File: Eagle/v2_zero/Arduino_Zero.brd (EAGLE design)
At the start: 81.3 x 36.8 mm, 73 parts, among them IC1 74HC125D, IC2 MAX31855, IC3 MAX31855, IC4 REG1117, IC5 ATSAMD21G-A, IC6 SPX3819-3.3, IC7 TXS0108E, IC8 TLP283, J3 USB-MICROB, J4 NM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

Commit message: update 3d packages
small updates
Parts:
- removed C18: 1uF, rcl:C0603K
- removed C20: 4.7uF, rcl:C0603K
- added C3, C9: TAJB106K020RNJ, microbuilder:CAPMP3528X210N
- IC8: device optocoupler:MINI-FLAT-4 -> gfe-hand-made:SO4_TOS
- moved IC8 53.6 mm to (8.41, -10.5)
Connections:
- net +5V: now also C9.1; no longer C20.1
- net 12V: now also C3.1; no longer C18.1
- net GND: now also C3.2, C9.2; no longer C18.2, C20.2, IC8.2
- net N$12: no longer IC8.1
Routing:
- net N$32: track 2.73 -> 4.65 mm
- net N$14: track 7.97 -> 6.28 mm
- net +5V: track 185.5 -> 186.6 mm
- net 12V: track 64.7 -> 65.8 mm
- net N$12: track 19.8 -> 18.9 mm
- net D5_LCD_DB5: track 28.4 -> 27.9 mm

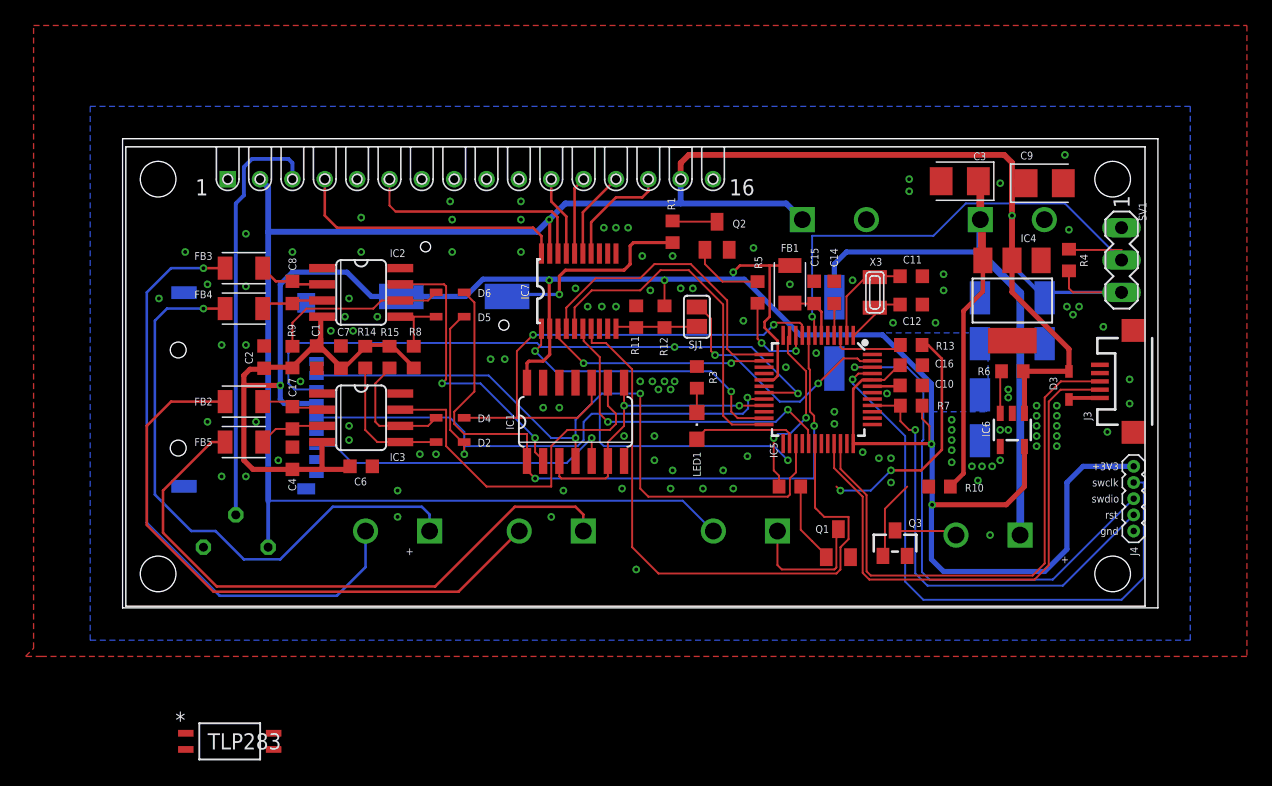
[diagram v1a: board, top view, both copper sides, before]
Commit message: schematic update
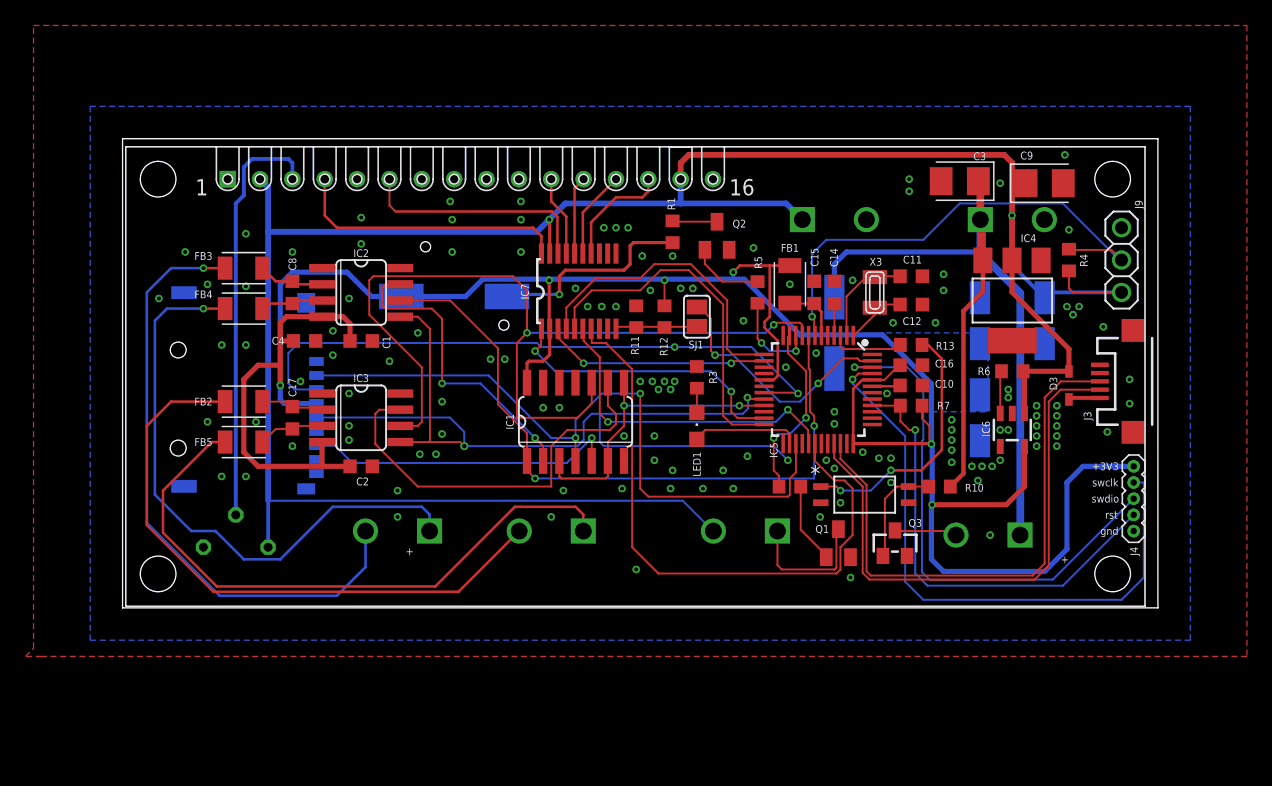
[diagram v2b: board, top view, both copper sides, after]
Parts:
- removed C6, C7: 10uF, rcl:C0603K
- removed D2, D4, D5, D6: 1N4148, adafruit:SOD323
- removed R14, R15, R8, R9: 10K, rcl:R0603
- removed SV1: (no value), con-lstb:MA03-1
- added J9: (no value), adafruit:1X03
- moved IC8 53.5 mm to (58.3, 8.89)
- moved C2 11.5 mm to (18.7, 11.1), turned to 0 degrees
- moved C4 9.26 mm to (14.3, 21.0), turned to 0 degrees
- moved C1 3.72 mm to (18.7, 21.0), turned to 0 degrees
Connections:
- removed net CS1: D4.2, IC3.6, R15.2
- removed net CS2: D6.2, IC2.6, R9.2
- removed net SCK1: D5.2, IC2.5, R8.2
- removed net SCK2: D2.2, IC3.5, R14.2
- net +3V3: no longer C6.1, C7.1, R14.1, R15.1, R8.1, R9.1
- net +5V: now also J9.3; no longer SV1.3
- net A1_BTN: now also J9.2; no longer SV1.2
- net A2_TC1_CS: now also IC2.6; no longer D6.1
- net A3_TC2_CS: now also IC3.6; no longer D4.1
- net GND: now also IC8.2, J9.1; no longer C6.2, C7.2, SV1.1
- net N$12: now also IC8.1
- net SCK: now also IC2.5, IC3.5; no longer D2.1, D5.1
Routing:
- net A3_TC2_CS: track 41.7 -> 68.8 mm
- net CS2: track 14.1 -> 0.00 mm
- net SCK2: track 10.8 -> 0.00 mm
- net CS1: track 9.86 -> 0.00 mm
- net +3V3: track 201.9 -> 194.4 mm
- net SCK1: track 5.14 -> 0.00 mm
- net SCK: track 69.9 -> 74.1 mm
- net N$18: track 28.5 -> 32.1 mm
- net N$14: track 6.28 -> 8.44 mm
- net N$7: track 22.6 -> 24.3 mm
- net A1_BTN: track 40.1 -> 38.8 mm
- net N$12: track 18.9 -> 20.1 mm

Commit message: schematic optimization
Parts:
- C1, C2: value 10uF -> 100n
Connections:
- net N$29 renamed XIN32
- net N$31 renamed XOUT32
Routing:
- net +3V3: track 194.4 -> 197.9 mm, vias 6 -> 8
- net XIN32: track 5.13 -> 7.68 mm

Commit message: update
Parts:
- removed IC6: SPX3819-3.3, microbuilder:SOT23-5
- removed R6: 100k, rcl:R0603
- added IC9: REG1117-5, gfe-hand-made:DCY0004A_N
- C5: value 2.2 µF -> TAJB106K020RNJ; device Wurth_Capacitors_WCAP-ASLI:WCAP-ASLI_4X5.5(DXL) -> microbuilder:CAPMP3528X210N
- IC4: value REG1117 -> REG1117-3.3; device burr-brown:SOT223 -> gfe-hand-made:DCY0004A_N
- R3: value (none) -> 470R
- R7: value (none) -> 10k
- moved FB4 19.5 mm to (28.9, 25.4), turned to 90 degrees
- moved FB3 16.7 mm to (26.2, 25.4), turned to 90 degrees
- moved J7 12.1 mm to (21.6, 6.03)
- moved J6 10.3 mm to (31.9, 6.03)
- moved IC4 8.89 mm to (69.8, 15.2), turned to 270 degrees
- moved C5 8.11 mm to (72.5, 8.73), flipped to the top, turned to 0 degrees
- moved FB2 3.67 mm to (8.41, 12.7), turned to 90 degrees
- moved FB5 1.77 mm to (11.3, 12.7), turned to 90 degrees
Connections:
- net D0_RX renamed !ETH_RST
- net D12 renamed ETH_CS
- net D1_TX renamed ETH_IRQ
- removed net EN: IC6.3, R6.2
- net +3V3: now also IC4.2, IC4.4; no longer IC6.5
- net +5V: now also IC4.3, IC9.2, IC9.4; no longer IC4.2, IC6.1, R6.1
- net 12V: now also IC9.3; no longer IC4.3
- net GND: now also IC9.1; no longer IC6.2
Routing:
- net MISO: track 24.0 -> 61.1 mm, vias 2 -> 4
- net N$11: track 48.1 -> 13.4 mm
- net N$20: track 48.3 -> 19.2 mm, vias 1 -> 2
- net N$22: track 46.5 -> 21.6 mm, vias 1 -> 3
- net N$15: track 48.6 -> 25.5 mm, vias 0 -> 1
- net N$27: track 4.92 -> 20.7 mm
- net N$21: track 5.18 -> 17.5 mm, vias 0 -> 2
- net +5V: track 186.6 -> 175.4 mm
- net +3V3: track 197.9 -> 193.1 mm, vias 8 -> 6
- net EN: track 3.35 -> 0.00 mm
- net N$13: track 5.29 -> 8.33 mm
- net A2_TC1_CS: track 54.0 -> 56.4 mm
- net D7_LCD_DB7: track 48.5 -> 47.1 mm, vias 0 -> 2
- net RS: track 21.9 -> 20.6 mm
- net E: track 18.5 -> 17.4 mm
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- added copper zone on layer 1, net +3V3
- added copper zone on layer 1, net +5V
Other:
- board text added: "SJ1 open and R11 NM for IC7 always on"
- board text added: "reflow_zero_v2 - gmammarella 2022"
